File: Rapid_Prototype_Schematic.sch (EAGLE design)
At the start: 162 parts, among them IC2 SI4459ADY-T1-GE3, IC8 SI4485DY-T1-GE3, J1 XT60-M, J10 XT60-M, J2 XT60-M, J4 UJ2-MIBH-2-SMT-TR-67, J5 XT60-M, J6 XT60-M, J7 XT60-M, J8 XT60-M, J9 XT60-M, Q1 LTV-8141S, Q10 SI4435DDY, Q11 DMN65D8LFB-7, Q12 SI4435DDY, Q13 DMN65D8LFB-7, Q14 SI4435DDY, Q15 DMN65D8LFB-7, Q3 DMN65D8LFB-7, Q4 SI4435DDY, Q5 DMN65D8LFB-7, Q6 SI4435DDY, Q7 DMN65D8LFB-7, Q8 SI4435DDY, Q9 DMN65D8LFB-7, U1 LM35DM, U2 LM2904ITPX/NOPB, U3 LM2904ITPX/NOPB, U4 LM2904ITPX/NOPB, U5 LM2904ITPX/NOPB, U6 LM2904ITPX/NOPB, U7 TLV1117LV33DCYR, U8 LT1374IS8-5PBF

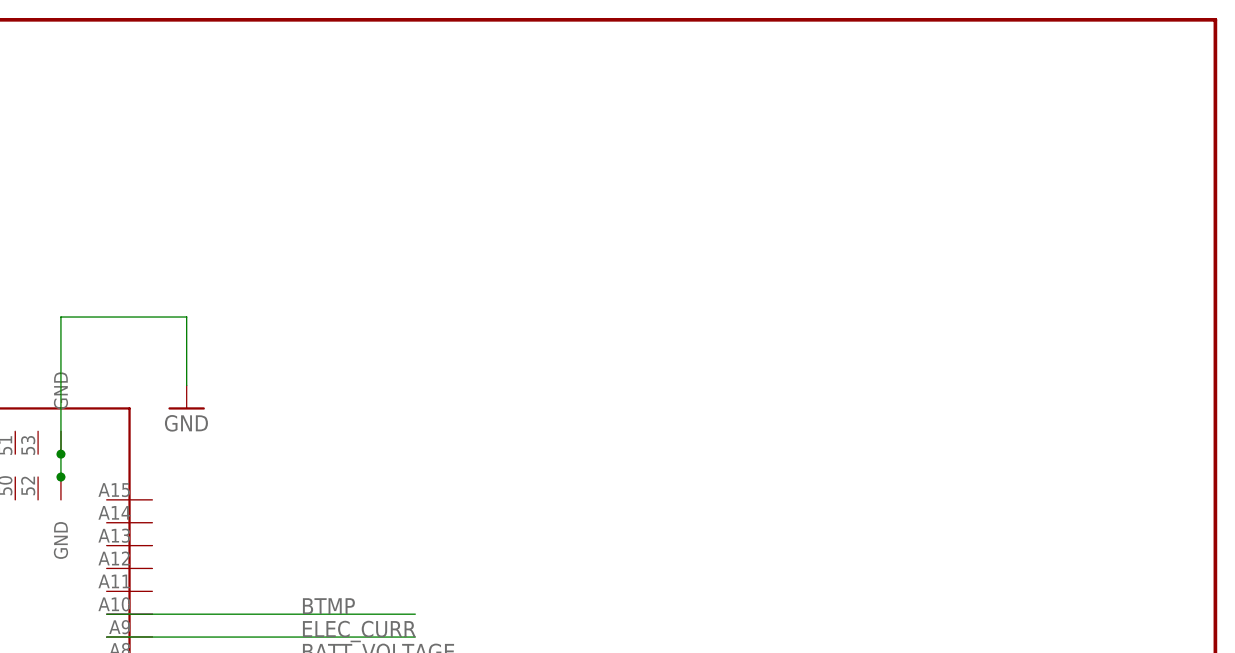
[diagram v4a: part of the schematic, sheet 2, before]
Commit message: Buck Regulators, Switches Regulators and Qwiic Connectors
Added Board connections for the Buck Regulators and added Qwiic Connectors on schematic.
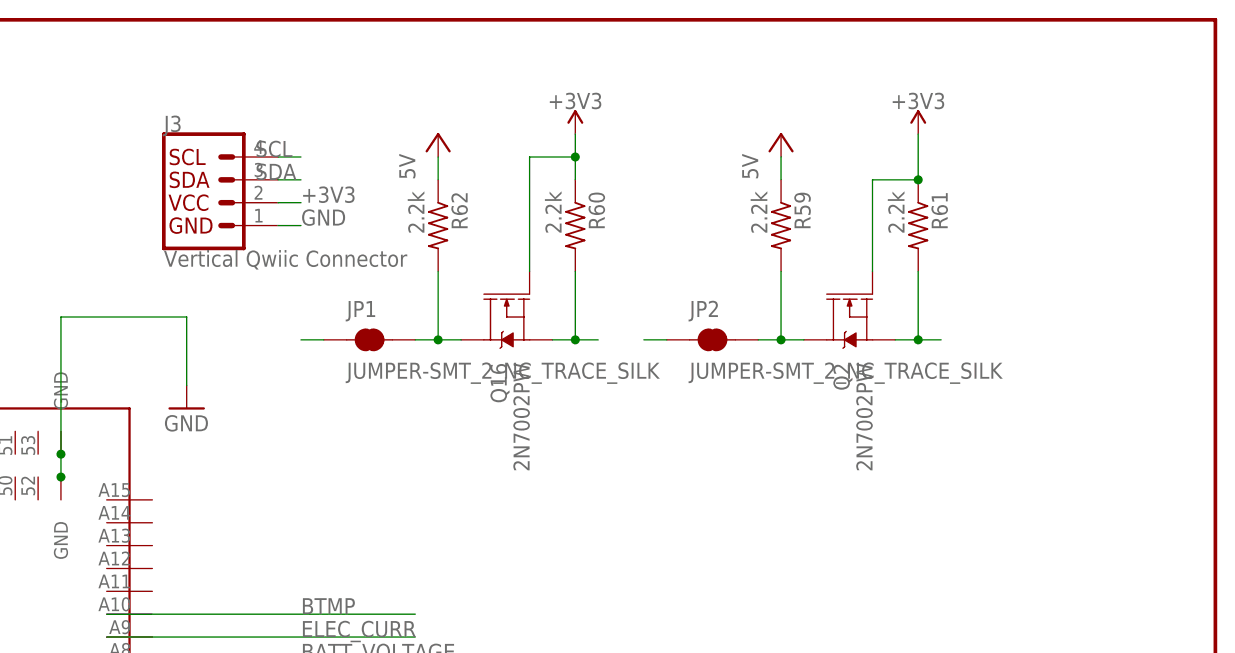
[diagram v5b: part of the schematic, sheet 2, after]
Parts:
- added J3: Vertical Qwiic Connector, SparkFun-Connectors:QWIIC_CONNECTOR
- added JP1, JP2: JUMPER-SMT_2_NC_TRACE_SILK, SparkFun-Jumpers:JUMPER-SMT_2_NC_TRACE_SILK
- added Q16, Q2: 2N7002PW, SparkFun-DiscreteSemi:MOSFET-NCH-2N7002PW
- added R59, R60, R61, R62: 2.2k, adafruit:R-US_R0805
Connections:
- new net +5V: R59.1, R62.1
- new net 3.3V: Q16.G, Q2.G, R60.1, R61.1
- new net N$14: JP2.2, Q2.D, R59.2
- new net N$28: Q2.S, R61.2
- new net N$40: JP1.2, Q16.D, R62.2
- new net N$41: Q16.S, R60.2
- new net N$42: JP1.1
- new net N$8: JP2.1
- net +3V3: now also J3.2
- net GND: now also J3.1
- net SCL: now also J3.4
- net SDA: now also J3.3

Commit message: Finished Routing
We focused on the quick QWIIC connector logic level conversion. We did libary work (it was intence)
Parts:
- removed JP1, JP2: JUMPER-SMT_2_NC_TRACE_SILK, SparkFun-Jumpers:JUMPER-SMT_2_NC_TRACE_SILK
- D3: value BOURNS_INC._SMAJ15ABOURNS_INC._SMAJ15A_0_0 -> BOURNS-INC.---SMAJ15A_BOURNS_INC._SMAJ15ABOURNS_INC._SMAJ15A_0_0; device Bourns Inc. - SMAJ15A:BOURNS_INC._SMAJ15ABOURNS_INC._SMAJ15A_0_0 -> Rapid_Prototype_Schematic:BOURNS-INC.---SMAJ15A_BOURNS_INC._SMAJ15ABOURNS_INC._SMAJ15A_0_0
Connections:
- removed net N$14: JP2.2, Q2.D, R59.2
- removed net N$28: Q2.S, R61.2
- removed net N$40: JP1.2, Q16.D, R62.2
- removed net N$41: Q16.S, R60.2
- removed net N$42: JP1.1
- removed net N$8: JP2.1
- new net SCL_3V3: J3.4, Q2.S, R61.2
- new net SDA_3V3: J3.3, Q16.S, R60.2
- net SCL: now also Q2.D, R59.2; no longer J3.4
- net SDA: now also Q16.D, R62.2; no longer J3.3
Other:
- note removed: "File History/Front page"

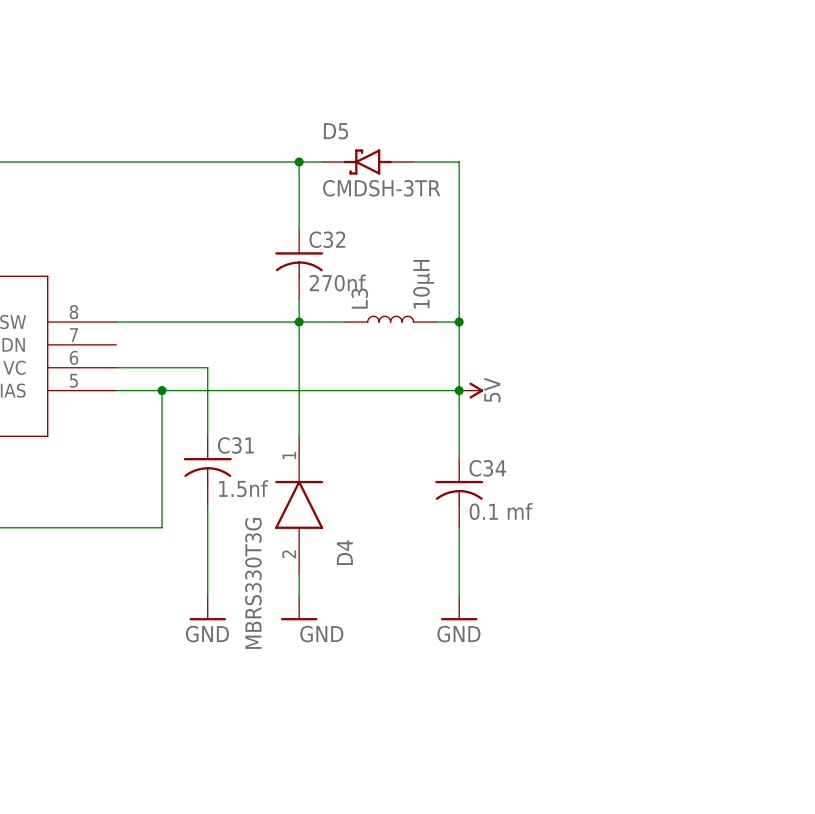
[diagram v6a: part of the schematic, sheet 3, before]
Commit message: Added Regulator Library, and Regulator to the Level shifter
Changed 5 volt traces from 0.008 to 0.02 for more flow.
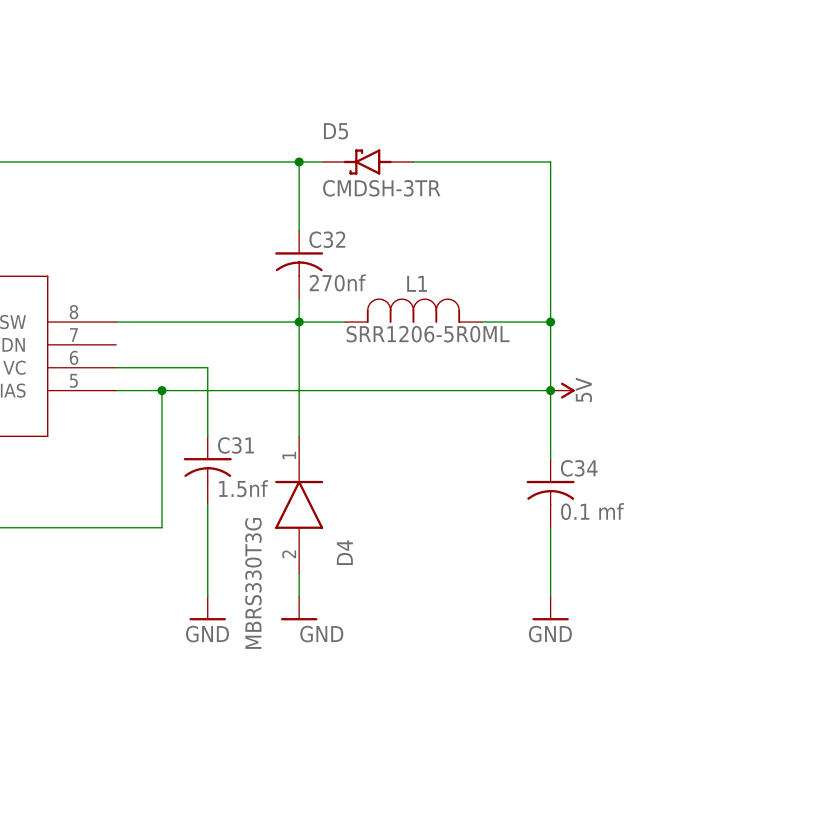
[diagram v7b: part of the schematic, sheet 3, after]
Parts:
- removed L3: 10μH, SparkFun-Coils:10μH_SHIELDED_INDUCTOR0805
- added L1: SRR1206-5R0ML, INDUCTOR_SRR1240:SRR1206-5R0ML
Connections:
- net 5V: now also L1.1; no longer L3.2
- net N$3: now also L1.2; no longer L3.1
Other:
- moved on the sheet: C34
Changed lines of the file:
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@@
 <setting verticaltext="up"/>
 </settings>
-<grid distance="0.1" unitdist="inch" unit="inch" style="lines" multiple="1" display="no" altdistance="0.01" altunitdist="inch" altunit="inch"/>
+<grid distance="0.1" unitdist="inch" unit="inch" style="lines" multiple="1" display="yes" altdistance="0.01" altunitdist="inch" altunit="inch"/>
 <layers>
 <layer number="1" name="Top" color="4" fill="1" visible="no" active="no"/>
@@
 <part name="TETHER" library="pinhead" library_urn="urn:adsk.eagle:library:325" deviceset="PINHD-1X2" device="" package3d_urn="urn:adsk.eagle:package:22435/2"/>
 <part name="U$1" library="tenda" deviceset="TENDA" device=""/>
-<part name="L3" library="SparkFun-Coils" deviceset="10μH_SHIELDED_INDUCTOR" device="0805" value="10μH"/>
 <part name="L2" library="SparkFun-Coils" deviceset="INDUCTOR" device=""/>
 <part name="J3" library="SparkFun-Connectors" deviceset="QWIIC_CONNECTOR" device="" value="Vertical Qwiic Connector"/>
@@
 <part name="SUPPLY3" library="SparkFun-PowerSymbols" deviceset="3.3V" device="" value="+3V3"/>
 <part name="SUPPLY5" library="SparkFun-PowerSymbols" deviceset="3.3V" device="" value="+3V3"/>
+<part name="L1" library="INDUCTOR_SRR1240" deviceset="SRR1206-5R0ML" device=""/>
 </parts>
 <sheets>
@@
 <attribute name="VALUE" x="22.86" y="-111.76" size="1.778" layer="96"/>
 </instance>
-<instance part="GND70" gate="1" x="147.32" y="-111.76" smashed="yes">
-<attribute name="VALUE" x="144.78" y="-114.3" size="1.778" layer="96"/>
+<instance part="GND70" gate="1" x="157.48" y="-111.76" smashed="yes">
+<attribute name="VALUE" x="154.94" y="-114.3" size="1.778" layer="96"/>
 </instance>
 <instance part="GND73" gate="1" x="10.16" y="-109.22" smashed="yes">
@@
 <attribute name="VALUE" x="-16.516859375" y="-81.666259375" size="1.7812" layer="96"/>
 </instance>
-<instance part="SUPPLY14" gate="G$1" x="147.32" y="-86.36" smashed="yes" rot="R270">
-<attribute name="VALUE" x="150.114" y="-86.36" size="1.778" layer="96" rot="R270" align="bottom-center"/>
+<instance part="SUPPLY14" gate="G$1" x="157.48" y="-86.36" smashed="yes" rot="R270">
+<attribute name="VALUE" x="160.274" y="-86.36" size="1.778" layer="96" rot="R270" align="bottom-center"/>
 </instance>
 <instance part="C29" gate="G$1" x="10.16" y="-96.52" smashed="yes">
@@
 <attribute name="VALUE" x="120.396" y="-98.171" size="1.778" layer="96"/>
 </instance>
-<instance part="C34" gate="G$1" x="147.32" y="-96.52" smashed="yes">
-<attribute name="NAME" x="148.336" y="-95.885" size="1.778" layer="95"/>
-<attribute name="VALUE" x="148.336" y="-100.711" size="1.778" layer="96"/>
+<instance part="C34" gate="G$1" x="157.48" y="-96.52" smashed="yes">
+<attribute name="NAME" x="158.496" y="-95.885" size="1.778" layer="95"/>
+<attribute name="VALUE" x="158.496" y="-100.711" size="1.778" layer="96"/>
 </instance>
 <instance part="C32" gate="G$1" x="129.54" y="-71.12" smashed="yes">
@@
 <attribute name="VALUE" x="146.05" y="50.8" size="1.778" layer="96" align="center-left"/>
 </instance>
-<instance part="L3" gate="G$1" x="139.7" y="-78.74" smashed="yes" rot="R90">
-<attribute name="NAME" x="137.16" y="-77.47" size="1.778" layer="95" font="vector" rot="R90"/>
-<attribute name="VALUE" x="142.24" y="-77.47" size="1.778" layer="96" font="vector" rot="R90" align="top-left"/>
-</instance>
 <instance part="L2" gate="G$1" x="58.42" y="0" smashed="yes" rot="R90">
 <attribute name="NAME" x="55.88" y="1.27" size="1.778" layer="95" font="vector" rot="R90"/>
 <attribute name="VALUE" x="60.96" y="1.27" size="1.778" layer="96" font="vector" rot="R90" align="top-left"/>
+</instance>
+<instance part="L1" gate="A" x="134.62" y="-78.74" smashed="yes">
+<attribute name="VALUE" x="134.6708" y="-80.9752" size="1.778" layer="96" ratio="10" rot="SR0"/>
+<attribute name="NAME" x="141.3256" y="-75.3872" size="1.778" layer="95" ratio="10" rot="SR0"/>
 </instance>
 </instances>
@@
 <pinref part="GND70" gate="1" pin="GND"/>
 <pinref part="C34" gate="G$1" pin="2"/>
-<wire x1="147.32" y1="-101.6" x2="147.32" y2="-109.22" width="0.1524" layer="91"/>
+<wire x1="157.48" y1="-101.6" x2="157.48" y2="-109.22" width="0.1524" layer="91"/>
 </segment>
 <segment>
@@
 <segment>
 <pinref part="D5" gate="G$1" pin="A"/>
-<wire x1="142.24" y1="-60.96" x2="147.32" y2="-60.96" width="0.1524" layer="91"/>
-<wire x1="147.32" y1="-60.96" x2="147.32" y2="-78.74" width="0.1524" layer="91"/>
-<wire x1="144.78" y1="-78.74" x2="147.32" y2="-78.74" width="0.1524" layer="91"/>
-<junction x="147.32" y="-78.74"/>
-<wire x1="147.32" y1="-78.74" x2="147.32" y2="-86.36" width="0.1524" layer="91"/>
-<junction x="147.32" y="-86.36"/>
+<wire x1="142.24" y1="-60.96" x2="157.48" y2="-60.96" width="0.1524" layer="91"/>
+<wire x1="157.48" y1="-60.96" x2="157.48" y2="-78.74" width="0.1524" layer="91"/>
+<junction x="157.48" y="-78.74"/>
+<wire x1="157.48" y1="-78.74" x2="157.48" y2="-86.36" width="0.1524" layer="91"/>
+<junction x="157.48" y="-86.36"/>
 <pinref part="SUPPLY14" gate="G$1" pin="5V"/>
 <pinref part="U8" gate="A" pin="BIAS"/>
@@
 <wire x1="20.32" y1="-101.6" x2="114.3" y2="-101.6" width="0.1524" layer="91"/>
 <wire x1="114.3" y1="-101.6" x2="114.3" y2="-86.36" width="0.1524" layer="91"/>
-<wire x1="147.32" y1="-86.36" x2="114.3" y2="-86.36" width="0.1524" layer="91"/>
+<wire x1="157.48" y1="-86.36" x2="114.3" y2="-86.36" width="0.1524" layer="91"/>
 <junction x="114.3" y="-86.36"/>
 <pinref part="C34" gate="G$1" pin="1"/>
-<wire x1="147.32" y1="-86.36" x2="147.32" y2="-93.98" width="0.1524" layer="91"/>
-<pinref part="L3" gate="G$1" pin="2"/>
+<wire x1="157.48" y1="-86.36" x2="157.48" y2="-93.98" width="0.1524" layer="91"/>
+<pinref part="L1" gate="A" pin="1"/>
+<wire x1="157.48" y1="-78.74" x2="149.86" y2="-78.74" width="0.1524" layer="91"/>
 </segment>
 <segment>
@@
 <pinref part="U8" gate="A" pin="VSW"/>
 <wire x1="109.22" y1="-78.74" x2="129.54" y2="-78.74" width="0.1524" layer="91"/>
-<pinref part="L3" gate="G$1" pin="1"/>
 <pinref part="C32" gate="G$1" pin="2"/>
 <wire x1="129.54" y1="-78.74" x2="134.62" y2="-78.74" width="0.1524" layer="91"/>
@@
 <junction x="129.54" y="-78.74"/>
 <wire x1="129.54" y1="-78.74" x2="129.54" y2="-76.2" width="0.1524" layer="91"/>
-</segment>
-</net>
+<pinref part="L1" gate="A" pin="2"/>
+</segment>
+</net>

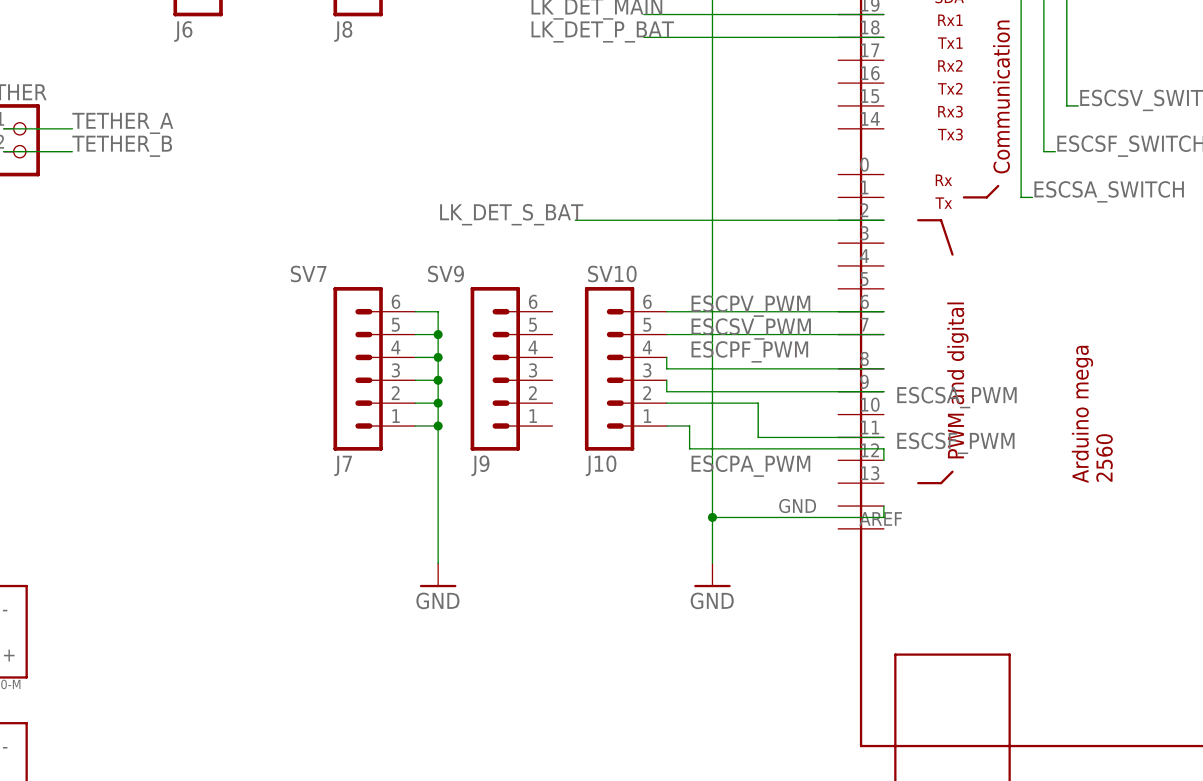
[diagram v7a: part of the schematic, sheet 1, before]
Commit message: Labeling and Part Replacing and GPIO LEDs
Switched PWM header with a different part, started labelling ESC's and added Software LED's
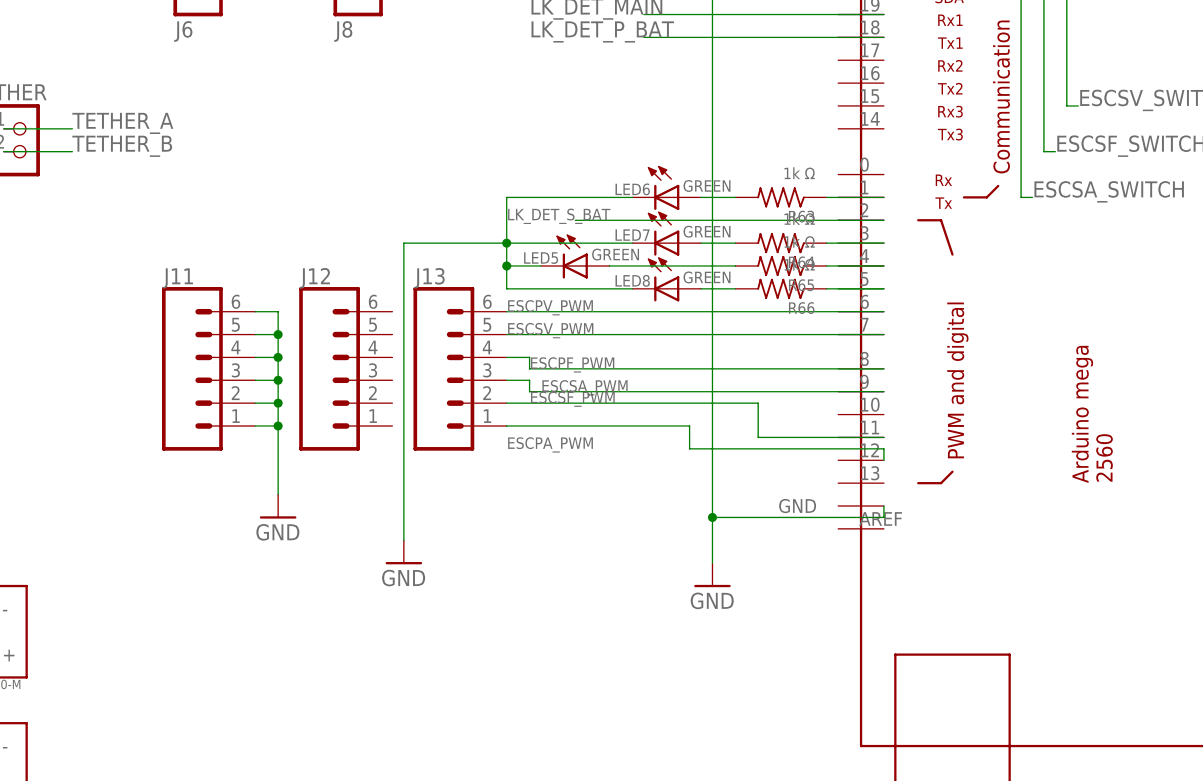
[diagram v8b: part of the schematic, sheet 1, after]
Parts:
- removed SV10: J10, con-lstb:MA06-1
- removed SV7: J7, con-lstb:MA06-1
- removed SV9: J9, con-lstb:MA06-1
- added J11, J12, J13: (no value), SparkFun-Connectors:CONN_06SILK_FEMALE_PTH
- added LED5, LED6, LED7, LED8: GREEN, adafruit:LEDCHIPLED_0805
- added R63, R64, R65, R66: 1k Ω, adafruit:R-US_M0805
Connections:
- new net N$14: $2_3_$_2020-06-04_21-52-10.4, R65.1
- new net N$28: $2_3_$_2020-06-04_21-52-10.5, R66.1
- new net N$40: $2_3_$_2020-06-04_21-52-10.1, R63.1
- new net N$41: LED6.A, R63.2
- new net N$42: LED7.A, R64.2
- new net N$45: LED5.A, R65.2
- new net N$46: LED8.A, R66.2
- new net N$8: $2_3_$_2020-06-04_21-52-10.3, R64.1
- net ESCPA_PWM: now also J13.1; no longer SV10.1
- net ESCPF_PWM: now also J13.4; no longer SV10.4
- net ESCPV_PWM: now also J13.6; no longer SV10.6
- net ESCSA_PWM: now also J13.3; no longer SV10.3
- net ESCSF_PWM: now also J13.2; no longer SV10.2
- net ESCSV_PWM: now also J13.5; no longer SV10.5
- net GND: now also J11.1, J11.2, J11.3, J11.4, J11.5, J11.6, LED5.C, LED6.C, LED7.C, LED8.C; no longer SV7.1, SV7.2, SV7.3, SV7.4, SV7.5, SV7.6
